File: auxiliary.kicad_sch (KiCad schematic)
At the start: 71 parts, among them IC1 MAX1708EEE+, J4 SM04B-SRSS-TB-LF-SN, J5 SM06B-SRSS-TB(LF)(SN), J6 SM09B-SRSS-TB(LF)(SN), Q1 BSS138AKA, U1 PCA9547BS,118, U2 NTS0102DP

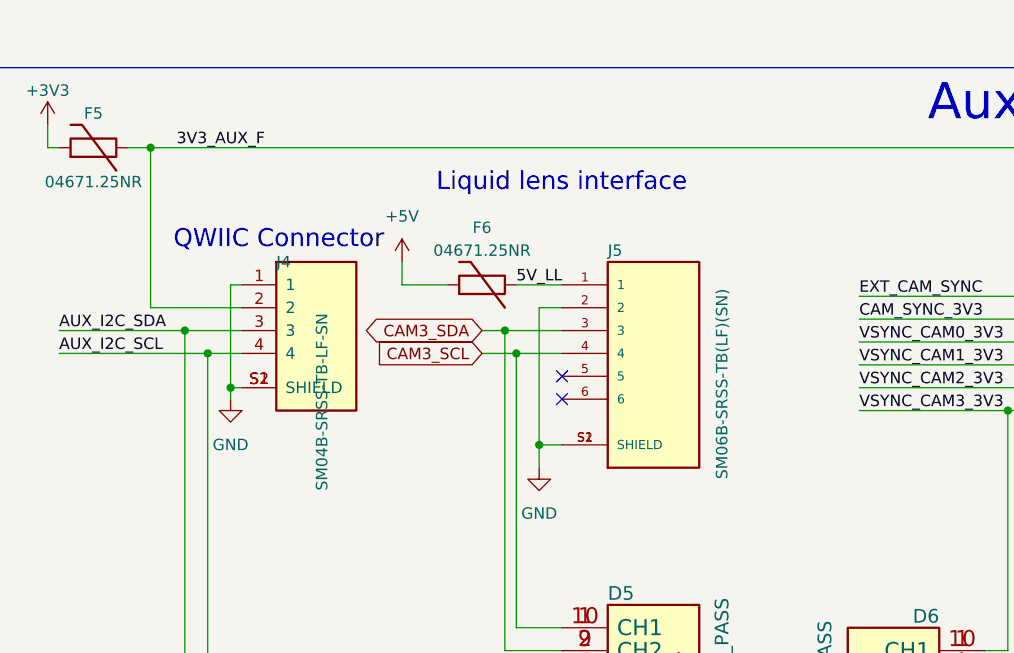
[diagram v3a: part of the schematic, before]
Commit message: Fixed bottom silkscreen
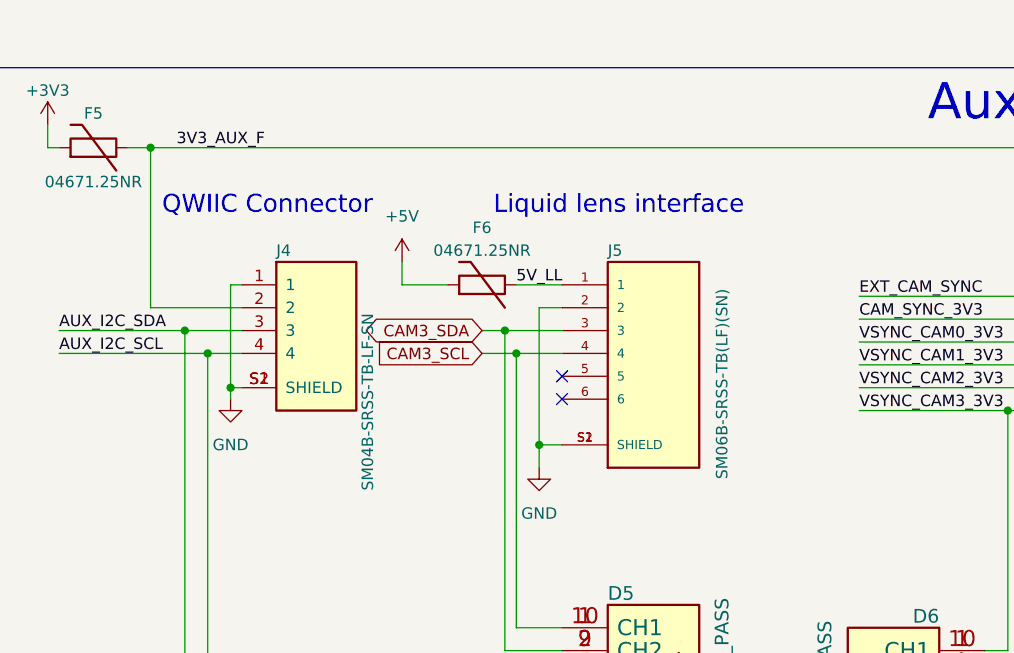
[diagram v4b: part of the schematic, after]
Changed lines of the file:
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@@
     (effects (font (size 1.27 1.27)) (justify left bottom))
   )
-  (text "Liquid lens interface" (at 74.93 170.18 180)
+  (text "Liquid lens interface" (at 81.28 172.72 180)
     (effects (font (size 2 2)) (justify left bottom))
   )
@@
     (effects (font (size 4 4)) (justify left bottom))
   )
-  (text "QWIIC Connector" (at 45.72 176.53 0)
+  (text "QWIIC Connector" (at 44.45 172.72 0)
     (effects (font (size 2 2)) (justify left bottom))
   )
@@
   (symbol (lib_id "antmicroRectangularConnectorsHeadersMalePins:SM04B-SRSS-TB-LF-SN") (at 58.42 186.69 0) (unit 1)
     (in_bom yes) (on_board yes)
-    (property "Reference" "J4" (id 0) (at 57.15 177.8 0)
+    (property "Reference" "J4" (id 0) (at 57.15 176.53 0)
       (effects (font (size 1.27 1.27)) (justify left))
     )
-    (property "Value" "SM04B-SRSS-TB-LF-SN" (id 1) (at 62.23 203.2 90)
+    (property "Value" "SM04B-SRSS-TB-LF-SN" (id 1) (at 67.31 203.2 90)
       (effects (font (size 1.27 1.27)) (justify left))
     )

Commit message: Added loclib, updated README and added pdf schematic
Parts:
- C10: footprint antmicro-footprints:0603-cap -> antmicro-jetson-agx-csi-adapter-footprints:0603-cap; symbol antmicroCapacitors0603:C_220n_0603 -> antmicro-jetson-agx-csi-adapter:C_220n_0603
- C11, C9: footprint antmicro-footprints:0603-cap -> antmicro-jetson-agx-csi-adapter-footprints:0603-cap; symbol antmicroCapacitors0603:C_100n_0603 -> antmicro-jetson-agx-csi-adapter:C_100n_0603
- C12, C8: footprint antmicro-footprints:1206-cap -> antmicro-jetson-agx-csi-adapter-footprints:1206-cap; symbol antmicroCapacitorsmisc:C_220u_1206_6V3 -> antmicro-jetson-agx-csi-adapter:C_220u_1206_6V3
- C5, C6, C7: footprint antmicro-footprints:0402-cap -> antmicro-jetson-agx-csi-adapter-footprints:0402-cap; symbol antmicroCapacitors0402:C_100n_0402 -> antmicro-jetson-agx-csi-adapter:C_100n_0402
- D5, D6, D7: footprint antmicro-footprints:PUSB3F96X -> antmicro-jetson-agx-csi-adapter-footprints:PUSB3F96X; symbol antmicroTVSDiodes:PUSB3F96X_PASS -> antmicro-jetson-agx-csi-adapter:PUSB3F96X_PASS
- D8: footprint antmicro-footprints:DO-214AC -> antmicro-jetson-agx-csi-adapter-footprints:DO-214AC; symbol antmicroDiodesRectifiersSingle:B340A-13-F -> antmicro-jetson-agx-csi-adapter:B340A-13-F
- F5, F6: footprint antmicro-footprints:0603-Fuse-Littelfuse-0467 -> antmicro-jetson-agx-csi-adapter-footprints:0603-Fuse-Littelfuse-0467; symbol antmicroFuses:04671.25NR -> antmicro-jetson-agx-csi-adapter:04671.25NR
- IC1: footprint antmicro-footprints:QSOP-16_3.9x4.9mm_P0.635mm -> antmicro-jetson-agx-csi-adapter-footprints:QSOP-16_3.9x4.9mm_P0.635mm; symbol antmicroDCDCConverters:MAX1708EEE+ -> antmicro-jetson-agx-csi-adapter:MAX1708EEE+
- J4: footprint antmicro-footprints:SM04B-SRSS-TB-LF-SN -> antmicro-jetson-agx-csi-adapter-footprints:SM04B-SRSS-TB-LF-SN; symbol antmicroRectangularConnectorsHeadersMalePins:SM04B-SRSS-TB-LF-SN -> antmicro-jetson-agx-csi-adapter:SM04B-SRSS-TB-LF-SN
- J5: footprint antmicro-footprints:JST_SM06B-SRSS-TB(LF)(SN) -> antmicro-jetson-agx-csi-adapter-footprints:JST_SM06B-SRSS-TB(LF)(SN); symbol antmicroRectangularConnectorsHeadersMalePins:SM06B-SRSS-TB(LF)(SN) -> antmicro-jetson-agx-csi-adapter:SM06B-SRSS-TB(LF)(SN)
- J6: footprint antmicro-footprints:JST_SM09B-SRSS-TB(LF)(SN) -> antmicro-jetson-agx-csi-adapter-footprints:JST_SM09B-SRSS-TB(LF)(SN); symbol antmicroRectangularConnectorsHeadersMalePins:SM09B-SRSS-TB(LF)(SN) -> antmicro-jetson-agx-csi-adapter:SM09B-SRSS-TB(LF)(SN)
- L1: footprint antmicro-footprints:IHLP2525CZER -> antmicro-jetson-agx-csi-adapter-footprints:IHLP2525CZER; symbol antmicroFixedInductors:IHLP2525CZER2R2M01 -> antmicro-jetson-agx-csi-adapter:IHLP2525CZER2R2M01
- Q1: footprint antmicro-footprints:SOT-23-3 -> antmicro-jetson-agx-csi-adapter-footprints:SOT-23-3; symbol antmicroTransistorsFETsMOSFETsSingle:BSS138AKA -> antmicro-jetson-agx-csi-adapter:BSS138AKA
- R10, R13, R14, R15, R16, R23, R24, R25, R26, R27, R36, R37, R38, R39, R42, R7, R8, R9: footprint antmicro-footprints:0402-res -> antmicro-jetson-agx-csi-adapter-footprints:0402-res; symbol antmicroResistors0402:R_0R_0402 -> antmicro-jetson-agx-csi-adapter:R_0R_0402
- R11: footprint antmicro-footprints:0402-res -> antmicro-jetson-agx-csi-adapter-footprints:0402-res; symbol antmicroResistors0402:R_10k_0402 -> antmicro-jetson-agx-csi-adapter:R_10k_0402
- R12, R17, R18, R19, R20, R21, R28, R29, R30, R31, R32, R33, R41, R43: footprint antmicro-footprints:0402-res -> antmicro-jetson-agx-csi-adapter-footprints:0402-res; symbol antmicroResistors0402:R_2k_0402 -> antmicro-jetson-agx-csi-adapter:R_2k_0402
- R22: footprint antmicro-footprints:0805-res -> antmicro-jetson-agx-csi-adapter-footprints:0805-res; symbol antmicroResistorsmisc:R_0R_0805 -> antmicro-jetson-agx-csi-adapter:R_0R_0805
- R34, R35: footprint antmicro-footprints:0603-res -> antmicro-jetson-agx-csi-adapter-footprints:0603-res; symbol antmicroResistors0603:R_2k2_0603 -> antmicro-jetson-agx-csi-adapter:R_2k2_0603
- R40: footprint antmicro-footprints:0603-res -> antmicro-jetson-agx-csi-adapter-footprints:0603-res; symbol antmicroResistors0603:R_2R_0603 -> antmicro-jetson-agx-csi-adapter:R_2R_0603
- TP12, TP13, TP14, TP15, TP16, TP17, TP18, TP19, TP20, TP21, TP22, TP23: footprint antmicro-footprints:Testpoint_smd_0_75mm -> antmicro-jetson-agx-csi-adapter-footprints:Testpoint_smd_0_75mm; symbol antmicroTestPoints:TP_SMD_0_75MM -> antmicro-jetson-agx-csi-adapter:TP_SMD_0_75MM
- U1: footprint antmicro-footprints:HVQFN24 -> antmicro-jetson-agx-csi-adapter-footprints:HVQFN24; symbol antmicroLogicSignalSwitchesMultiplexersDecoders:PCA9547BS,118 -> antmicro-jetson-agx-csi-adapter:PCA9547BS,118
- U2: footprint antmicro-footprints:TSSOP-8_W3mm -> antmicro-jetson-agx-csi-adapter-footprints:TSSOP-8_W3mm; symbol antmicroLogicTranslatorsLevelShifters:NTS0102DP -> antmicro-jetson-agx-csi-adapter:NTS0102DP

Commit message: [#60956] WiP Update symbols references
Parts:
- C10: value C_220n_0402 -> C_220n_0603; footprint antmicro-jetson-agx-csi-adapter-footprints:0603-cap -> antmicro-footprints:C_0603_1608Metric; symbol antmicro-jetson-agx-csi-adapter:C_220n_0603 -> antmicroCapacitors0603:C_220n_0603; Author (none) -> Antmicro; License (none) -> Apache-2.0; Manufacturer WALSIN -> Walsin; Public (none) -> False
- C11, C9: value C_100n_0402 -> C_100n_0603; footprint antmicro-jetson-agx-csi-adapter-footprints:0603-cap -> antmicro-footprints:C_0603_1608Metric; symbol antmicro-jetson-agx-csi-adapter:C_100n_0603 -> antmicroCapacitors0603:C_100n_0603; Author (none) -> Antmicro; License (none) -> Apache-2.0; Public (none) -> False
- C12, C8: value C_220u_KEMET_D -> C_220u_1206_6V3; footprint antmicro-jetson-agx-csi-adapter-footprints:1206-cap -> antmicro-footprints:C_1206_3216Metric; symbol antmicro-jetson-agx-csi-adapter:C_220u_1206_6V3 -> antmicroCapacitorsmisc:C_220u_1206_6V3; Author (none) -> Antmicro; License (none) -> Apache-2.0; Public (none) -> False
- C5, C6, C7: footprint antmicro-jetson-agx-csi-adapter-footprints:0402-cap -> antmicro-footprints:C_0402_1005Metric; symbol antmicro-jetson-agx-csi-adapter:C_100n_0402 -> antmicroCapacitors0402:C_100n_0402; Author (none) -> Antmicro; Dielectric (none) -> X5R; License (none) -> Apache-2.0; Public (none) -> False; Voltage (none) -> 50V
- D5, D6, D7: footprint antmicro-jetson-agx-csi-adapter-footprints:PUSB3F96X -> antmicro-footprints:Nexperia_DFN-10_2.5x1mm_P0.5mm; symbol antmicro-jetson-agx-csi-adapter:PUSB3F96X_PASS -> antmicroTVSDiodes:PUSB3F96X_PASS; Author (none) -> Antmicro; License (none) -> Apache-2.0
- F5, F6: footprint antmicro-jetson-agx-csi-adapter-footprints:0603-Fuse-Littelfuse-0467 -> antmicro-footprints:F_0603_1608Metric; symbol antmicro-jetson-agx-csi-adapter:04671.25NR -> antmicroFuses:F_1.25A_0603
- J5: footprint antmicro-jetson-agx-csi-adapter-footprints:JST_SM06B-SRSS-TB(LF)(SN) -> antmicro-footprints:Conn_JST_GH_1x6_SM06B-GHS-TB-LF-SN; symbol antmicro-jetson-agx-csi-adapter:SM06B-SRSS-TB(LF)(SN) -> antmicroWire2BoardConnectors:JST_GH_1x6_SM06B-GHS-TB-LF-SN
- J6: footprint antmicro-jetson-agx-csi-adapter-footprints:JST_SM09B-SRSS-TB(LF)(SN) -> antmicro-footprints:Conn_JST_SH_1x9_SM09B-SRSS-TB-LF-SN; symbol antmicro-jetson-agx-csi-adapter:SM09B-SRSS-TB(LF)(SN) -> antmicroWire2BoardConnectors:JST_SH_1x9_SM09B-SRSS-TB-LF-SN
- L1: footprint antmicro-jetson-agx-csi-adapter-footprints:IHLP2525CZER -> antmicro-footprints:L_2525_6363Metric; symbol antmicro-jetson-agx-csi-adapter:IHLP2525CZER2R2M01 -> antmicroFixedInductors:L_8u2_4A_2525
- Q1: footprint antmicro-jetson-agx-csi-adapter-footprints:SOT-23-3 -> antmicro-footprints:SOT-23-3; symbol antmicro-jetson-agx-csi-adapter:BSS138AKA -> antmicroTransistorsFETsMOSFETsSingle:BSS138AKA
- R10, R13, R14, R15, R16, R23, R24, R25, R26, R27, R36, R37, R38, R39, R42, R7, R8, R9: footprint antmicro-jetson-agx-csi-adapter-footprints:0402-res -> antmicro-footprints:R_0402_1005Metric; symbol antmicro-jetson-agx-csi-adapter:R_0R_0402 -> antmicroResistors0402:R_0R_0402
- R11: footprint antmicro-jetson-agx-csi-adapter-footprints:0402-res -> antmicro-footprints:R_0402_1005Metric; symbol antmicro-jetson-agx-csi-adapter:R_10k_0402 -> antmicroResistors0402:R_10k_0402
- R12, R17, R18, R19, R20, R21, R28, R29, R30, R31, R32, R33, R41, R43: footprint antmicro-jetson-agx-csi-adapter-footprints:0402-res -> antmicro-footprints:R_0402_1005Metric; symbol antmicro-jetson-agx-csi-adapter:R_2k_0402 -> antmicroResistors0402:R_2k_0402
- R22: footprint antmicro-jetson-agx-csi-adapter-footprints:0805-res -> antmicro-footprints:R_0805_2012Metric; symbol antmicro-jetson-agx-csi-adapter:R_0R_0805 -> antmicroResistorsmisc:R_0R_0805; Author (none) -> Antmicro; Current (none) -> 2.5A; License (none) -> Apache-2.0; Manufacturer VISHAY -> Vishay; Public (none) -> False
- R34, R35: footprint antmicro-jetson-agx-csi-adapter-footprints:0603-res -> antmicro-footprints:R_0603_1608Metric; symbol antmicro-jetson-agx-csi-adapter:R_2k2_0603 -> antmicroResistors0603:R_2k2_0603
- R40: footprint antmicro-jetson-agx-csi-adapter-footprints:0603-res -> antmicro-footprints:R_0603_1608Metric; symbol antmicro-jetson-agx-csi-adapter:R_2R_0603 -> antmicroResistors0603:R_2R_0603
- U1: footprint antmicro-jetson-agx-csi-adapter-footprints:HVQFN24 -> antmicro-footprints:VQFN-24-1EP_3.8x3.8x1.0mm_P0.5mm; symbol antmicro-jetson-agx-csi-adapter:PCA9547BS,118 -> antmicroLogicSignalSwitchesMultiplexersDecoders:PCA9547_VQFN
- U2: footprint antmicro-jetson-agx-csi-adapter-footprints:TSSOP-8_W3mm -> antmicro-footprints:TSSOP-8_3x3mm_P0.65mm; symbol antmicro-jetson-agx-csi-adapter:NTS0102DP -> antmicroLogicTranslatorsLevelShifters:NTS0102_TSSOP
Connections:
- net +1V8: now also C6.2; no longer C6.1
- net +3V3: now also C5.2, C7.2, C8.2; no longer C5.1, C7.1, C8.1
- net 5V_C: now also C12.2; no longer C12.1
- net GND: now also C10.2, C11.1, C12.1, C5.1, C6.1, C7.1, C8.1, C9.1; no longer C10.1, C11.2, C12.2, C5.2, C6.2, C7.2, C8.2, C9.2
- net at IC1.10 (OUT), IC1.15 (~{3.3}/5), IC1.16 (CLK)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: now also C11.2; no longer C11.1
- net at IC1.7 (SS/LIM): now also C9.2; no longer C9.1
- net at IC1.8 (REF): now also C10.1; no longer C10.2
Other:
- moved on the sheet: C10, C11, C12, C5, C6, C7, C8, C9

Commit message: [#60956] WiP Update symbols references
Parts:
- removed J4: SM04B-SRSS-TB-LF-SN, antmicro-jetson-agx-csi-adapter-footprints:SM04B-SRSS-TB-LF-SN, symbol antmicro-jetson-agx-csi-adapter:SM04B-SRSS-TB-LF-SN
- added J4: JST_SH_1x4_SM04B-SRSS-TB-LF-SN, antmicro-footprints:Conn_JST_SH_1x4_SM04B-SRSS-TB-LF-SN, symbol antmicroWire2BoardConnectors:JST_SH_1x4_SM04B-SRSS-TB-LF-SN
- F5, F6: value 04671.25NR -> F_1.25A_0603; Author (none) -> Antmicro; License (none) -> Apache-2.0; Manufacturer Littelfuse Inc. -> Littelfuse
- IC1: Manufacturer (none) -> Maxim Integrated
- J5: value SM06B-SRSS-TB(LF)(SN) -> JST_GH_1x6_SM06B-GHS-TB-LF-SN; Author (none) -> Antmicro; License (none) -> Apache-2.0; Manufacturer (none) -> JST Automotive Connectors
- J6: value SM09B-SRSS-TB(LF)(SN) -> JST_SH_1x9_SM09B-SRSS-TB-LF-SN; Author (none) -> Antmicro; License (none) -> Apache-2.0; Manufacturer (none) -> JST Automotive Connectors
- L1: value IHLP2525CZER2R2M01 -> L_8u2_4A_2525; Author (none) -> Antmicro; IMax (none) -> 4 A; ISat (none) -> 7.5 A; License (none) -> Apache-2.0; MaxCur 8A -> (none); Public (none) -> False; Val 2.2u -> 8u2/4A
- Q1: Author (none) -> Antmicro; License (none) -> Apache-2.0; MPN BSS138AKAR -> BSS138AKA; Public (none) -> False; now left out of the parts list
- R10, R13, R14, R15, R16, R23, R24, R25, R26, R27, R36, R37, R38, R39, R42, R8, R9: Author (none) -> Antmicro; Current (none) -> 1A; License (none) -> Apache-2.0; Manufacturer PANASONIC -> Panasonic; Public (none) -> False
- R11: Author (none) -> Antmicro; License (none) -> Apache-2.0; MPN CRCW040210K0FKEDHP -> CR0402-FX-1002GLF; Manufacturer VISHAY -> Bourns; Public (none) -> False; Tolerance (none) -> 1%
- R12, R17, R18, R19, R20, R21, R28, R29, R30, R31, R32, R33, R41, R43: Author (none) -> Antmicro; License (none) -> Apache-2.0; MPN CRCW04022K00FKED -> CR0402-FX-2001GLF; Manufacturer VISHAY -> Bourns; Public (none) -> False; Tolerance (none) -> 1%
- R34, R35: value R_2k_0402 -> R_2k2_0603; Author (none) -> Antmicro; License (none) -> Apache-2.0; MPN MCMR06X2201FTL -> CR0603-FX-2201ELF; Manufacturer MULTICOMP -> Bourns; Public (none) -> False; Tolerance (none) -> 1%
- R40: value R_2R_0402 -> R_2R_0603; Author (none) -> Antmicro; License (none) -> Apache-2.0; MPN MCSR06W2R00FTL -> CR0603-FX-2R00ELF; Manufacturer MULTICOMP -> Bourns; Public (none) -> False; Tolerance (none) -> 1%
- R7: Author (none) -> Antmicro; Current (none) -> 1A; DNP DNP -> (none); License (none) -> Apache-2.0; Manufacturer PANASONIC -> Panasonic; Public (none) -> False; now not fitted
- U1: value PCA9547BS,118 -> PCA9547_VQFN; Author (none) -> Antmicro; License (none) -> Apache-2.0; Manufacturer Nexperia -> NXP
- U2: value NTS0102DP -> NTS0102_TSSOP; Author (none) -> Antmicro; License (none) -> Apache-2.0; Manufacturer NXP Semiconductors -> NXP
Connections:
- net 3V3_AUX_F: now also J4.2
- net AUX_I2C_SCL: now also J4.4
- net AUX_I2C_SDA: now also J4.3
- net GND: now also J5.MP, J6.MP, J4.1, J4.MP; no longer J5.S1 (SHIELD), J5.S2 (SHIELD), J6.S1 (SHIELD), J6.S2 (SHIELD)
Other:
- moved on the sheet: C5, C7, R10, R11, R32, R33, R8, R9

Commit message: [#60956] WiP Update footprints
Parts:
- added MP1, MP2: MP_NPTH_Drill3.5mm, antmicro-footprints:MP_NPTH_Drill3.5mm, symbol antmicroMechanicalParts:MP_NPTH_Drill3.5mm
- added N1: antmicro_logo, antmicro-footprints:antmicro-logo_scaled_20mm, symbol antmicroMechanicalParts:antmicro_logo
- added N2: oshw_logo, antmicro-footprints:oshw-logo, symbol antmicroMechanicalParts:oshw_logo
- J5: value JST_GH_1x6_SM06B-GHS-TB-LF-SN -> SM06B-SRSS-TB(LF)(SN); footprint antmicro-footprints:Conn_JST_GH_1x6_SM06B-GHS-TB-LF-SN -> antmicro-jetson-agx-csi-adapter-footprints:JST_SM06B-SRSS-TB(LF)(SN); symbol antmicroWire2BoardConnectors:JST_GH_1x6_SM06B-GHS-TB-LF-SN -> antmicro-jetson-agx-csi-adapter:SM06B-SRSS-TB(LF)(SN); Author Antmicro -> (none); License Apache-2.0 -> (none); Manufacturer JST Automotive Connectors -> JST
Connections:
- net GND: now also J5.S1 (SHIELD), J5.S2 (SHIELD); no longer J5.MP
